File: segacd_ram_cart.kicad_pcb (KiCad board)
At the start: 4 copper layers, 92.6 x 63.7 mm, 16 parts, among them J1 Sega_MegaDrive_Cart_Conn, J2 AVR-JTAG-10, J3 Backup, U1 CY62148ELL-45ZSXI, U2 BQ2201SN, U3 ATF1502AS-xAx44

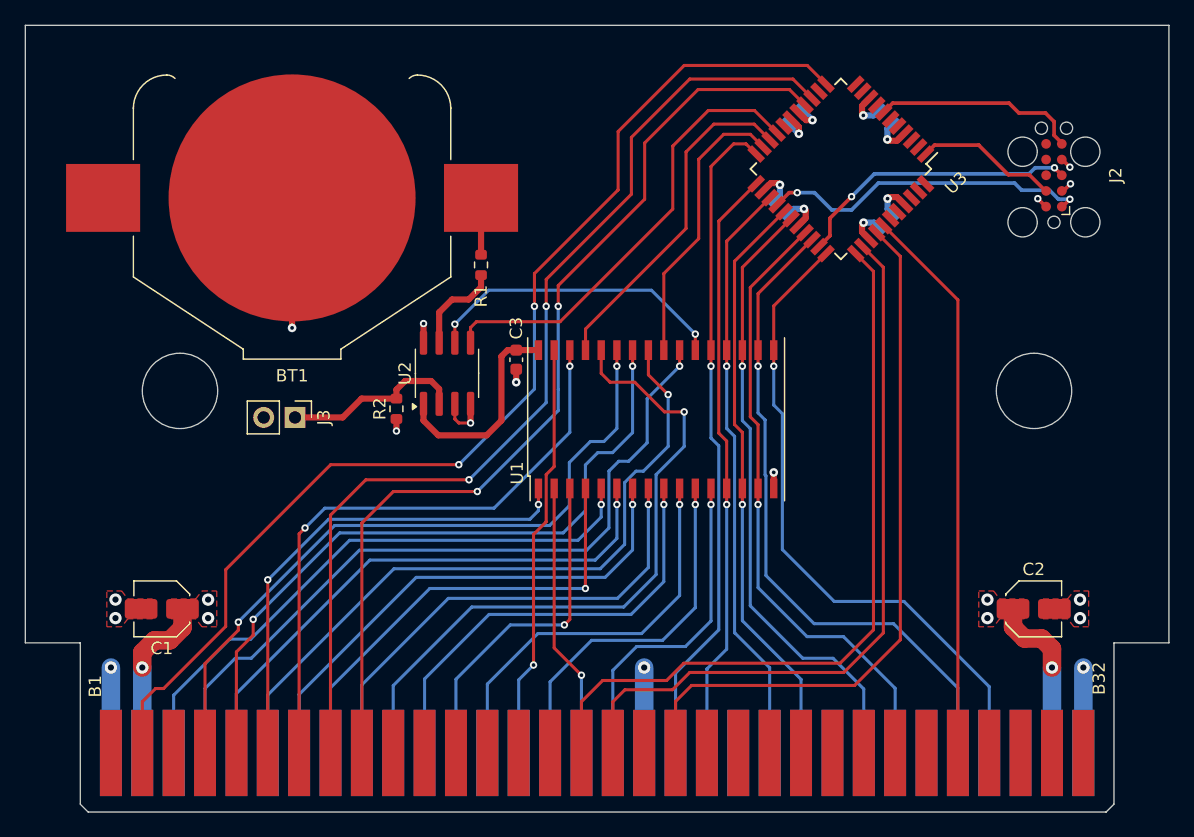
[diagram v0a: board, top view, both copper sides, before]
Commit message: Changed layout and updated symbols/footprints
* Changed the layout of components to allow for shrinking the board.
* Imported custom symbols and footprints into project library.
* Updated symbols and footprints to satisfy ERC/DRC checks.
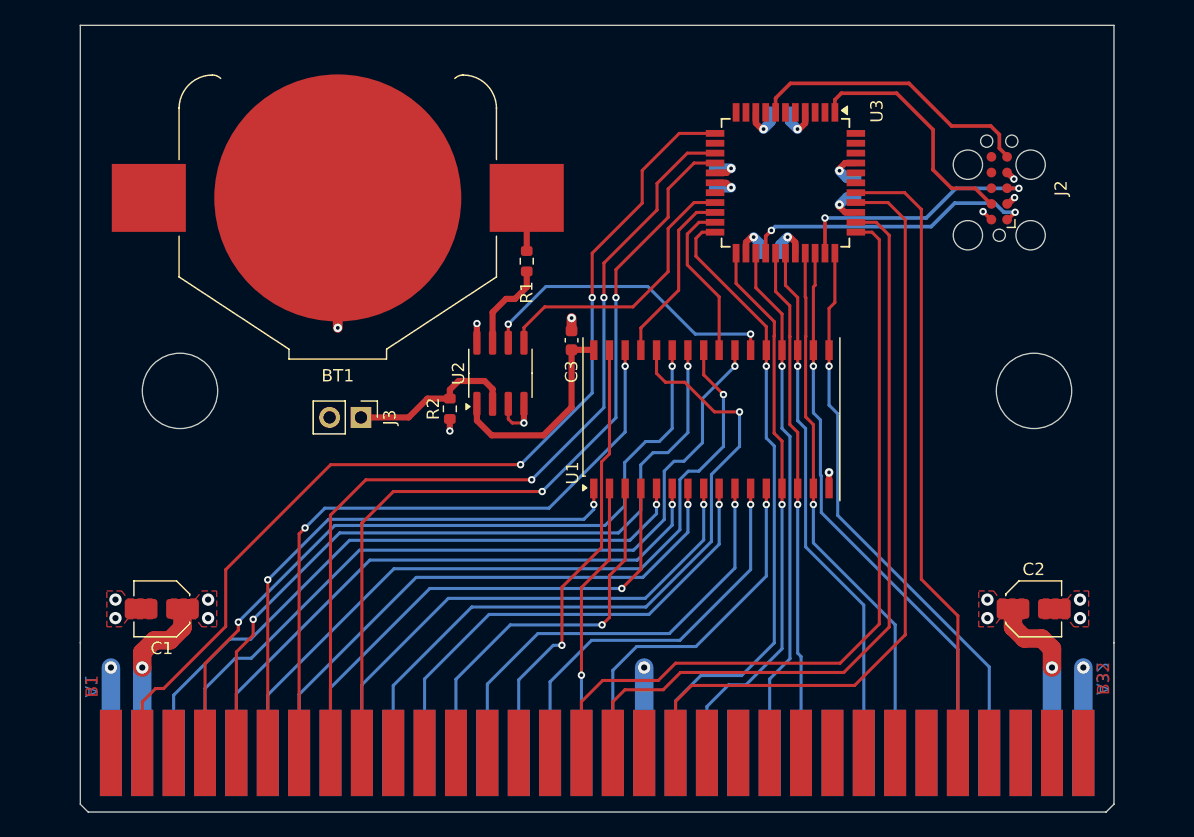
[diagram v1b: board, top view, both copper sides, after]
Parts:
- moved C6 8.64 mm to (124.8, 66.9), turned to 0 degrees
- moved C7 8.19 mm to (119.5, 72.2), turned to 90 degrees
- moved J3 5.34 mm to (90.8, 91.5)
- moved C3 4.75 mm to (107.9, 85.3), turned to 90 degrees
- moved U3 4.62 mm to (125.2, 72.5), turned to -90 degrees
- moved J2 4.55 mm to (142.5, 73.0)
- moved U1 4.48 mm to (119.2, 91.7)
- moved R2 4.33 mm to (98.0, 90.8)
- moved U2 4.33 mm to (102.1, 88.0)
- moved C9 3.76 mm to (130.9, 73.0), turned to -90 degrees
- moved C8 3.73 mm to (124.0, 78.2), turned to 180 degrees
- moved R1 3.71 mm to (104.2, 78.9)
- moved BT1 3.70 mm to (89.0, 73.8)
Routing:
- net /PL_~{CE}: track 37.1 -> 22.9 mm
- net /SR_~{WE}: track 27.7 -> 14.5 mm
- net /C_~{MRES}: track 92.4 -> 80.5 mm
- net /C_A20: track 82.1 -> 70.7 mm
- net /C_A21: track 78.2 -> 67.7 mm
- net /SR_~{OE}: track 23.1 -> 13.1 mm
- net /C_D4: track 53.8 -> 45.4 mm
- net /TDI: track 11.6 -> 19.5 mm
- net /C_D5: track 50.4 -> 43.1 mm
- net /C_D2: track 50.6 -> 43.5 mm
- net /TMS: track 16.8 -> 23.5 mm
- net /C_D3: track 52.7 -> 46.0 mm
- net /C_D1: track 47.7 -> 41.3 mm
- net /C_~{LWR}: track 45.2 -> 51.1 mm
- net /C_D6: track 47.9 -> 42.3 mm
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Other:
- board size 92.6 x 63.7 mm -> 83.7 x 63.7 mm
